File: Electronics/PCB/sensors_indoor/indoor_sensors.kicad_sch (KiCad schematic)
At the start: 31 parts, among them J3 B5B-ZR, Q1 DMN62D0U, U10 SPS30, U11 74LVC1G08, U4 LPS22DF, U5 SHT45-AD1F, U6 SCD41-D-R2, U7 SGP41, U8 OPT4001DTSR, U9 TSOP38436

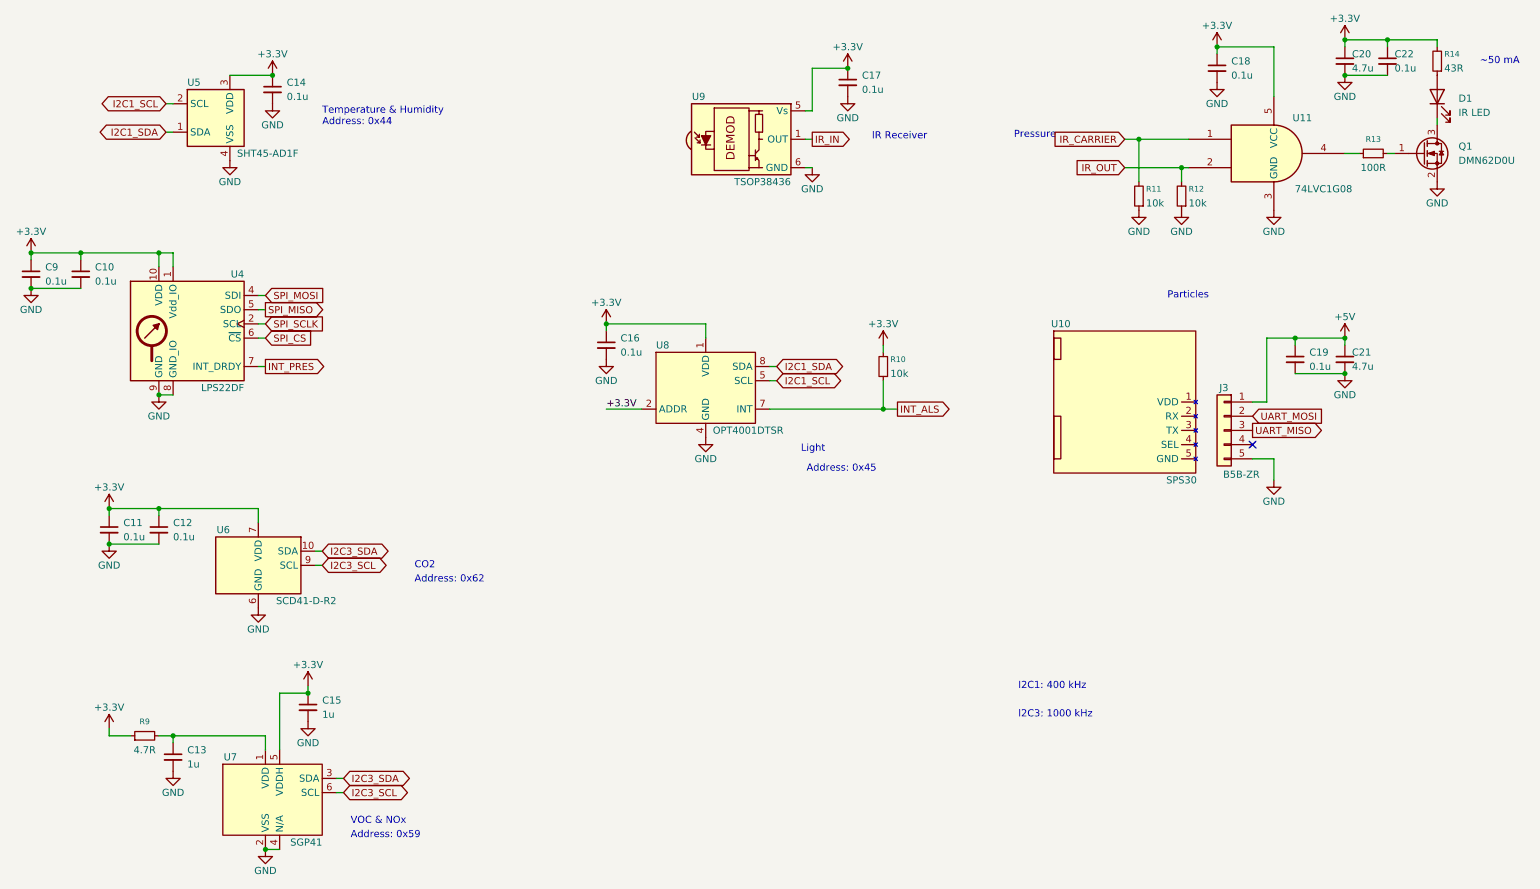
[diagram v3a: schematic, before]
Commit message: Completed schematic, done most routing
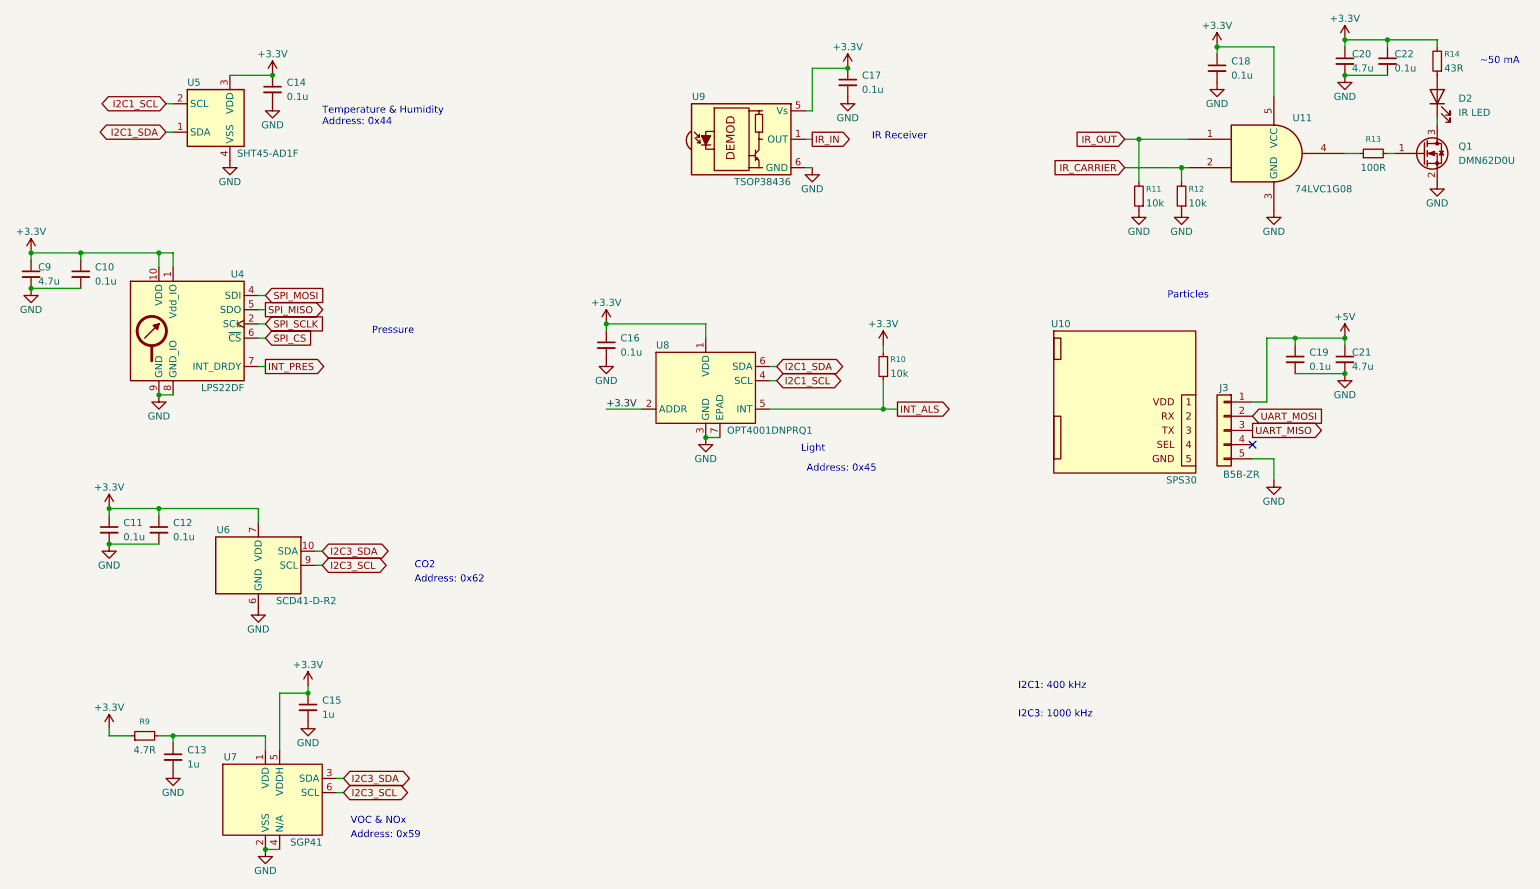
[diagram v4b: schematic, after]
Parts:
- C9: value 0.1u -> 4.7u; footprint Capacitor_SMD:C_0402_1005Metric -> Capacitor_SMD:C_0805_2012Metric
- U8: value OPT4001DTSR -> OPT4001DNPRQ1; footprint DWlib:TI_SOT-5X3_OPT4001DTSR -> DWlib:TI_USON-6-1EP_2x2mm_P0.5mm_EP0.65x1.35mm; symbol DWlib:OPT4001DTSR -> DWlib:OPT4001DNPRQ1; MPN (none) -> OPT4001DNPRQ1; Mouser PN (none) -> 595-OPT4001DNPRQ1
- renumbered D1 to D2
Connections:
- net GND: now also U8.3 (GND), U8.7 (EPAD); no longer U8.4 (GND)
- net I2C1_SCL: now also U8.4 (SCL); no longer U8.5 (SCL)
- net I2C1_SDA: now also U8.6 (SDA); no longer U8.8 (SDA)
- net INT_ALS: now also U8.5 (INT); no longer U8.7 (INT)
- net IR_CARRIER: now also R12.2, U11.2; no longer R11.2, U11.1
- net IR_OUT: now also R11.2, U11.1; no longer R12.2, U11.2

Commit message: Improved pressure sensor footprint
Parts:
- U4: footprint Package_LGA:ST_HLGA-10_2x2mm_P0.5mm_LayoutBorder3x2y -> DWlib:ST_HLGA-10L_2x2mm_P0.5mm_LayoutBorder3x2y
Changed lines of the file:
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@@
 			)
 		)
-		(property "Footprint" "Package_LGA:ST_HLGA-10_2x2mm_P0.5mm_LayoutBorder3x2y"
+		(property "Footprint" "DWlib:ST_HLGA-10L_2x2mm_P0.5mm_LayoutBorder3x2y"
 			(at 43.18 87.63 0)
 			(effects
